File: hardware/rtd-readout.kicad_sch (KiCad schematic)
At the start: 0 parts

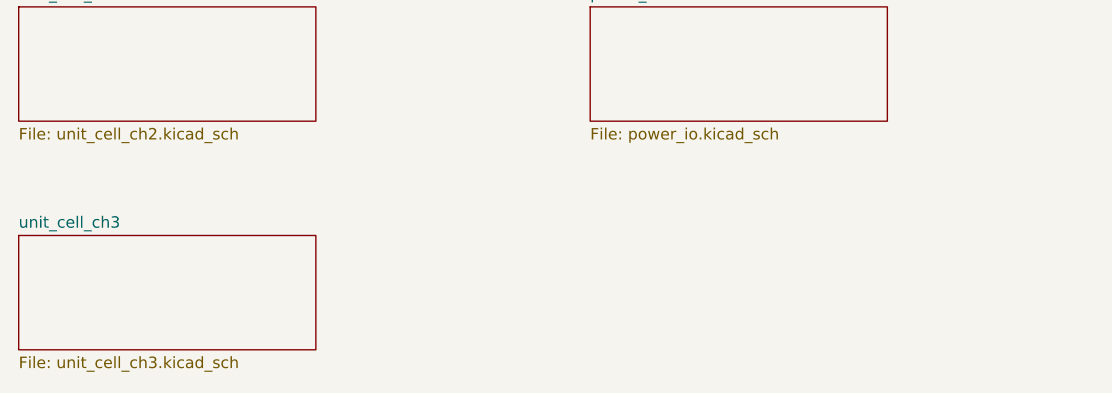
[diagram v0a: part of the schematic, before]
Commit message: trackE: record accepted 3-sheet deviation + clean loose reports artifacts
Integration-review housekeeping (no schematic logic change):
- Mark the three-sheet unit_cell structure as an ACCEPTED deviation in
  docs/sessions/trackE.md, with the consequence noted (a unit-cell change must
  be applied to all three sheets by hand).
- Add a one-line note in root rtd-readout.kicad_sch (title-block comment 2 +
  on-canvas text) so the next reader isn't surprised.
- Remove loose untracked reports/ gate artifacts so the tree is clean for merge.
ERC re-confirmed 0 errors / 0 warnings after the root-sheet edit.

Co-Authored-By: Claude Opus 4.8 <noreply@anthropic.com>
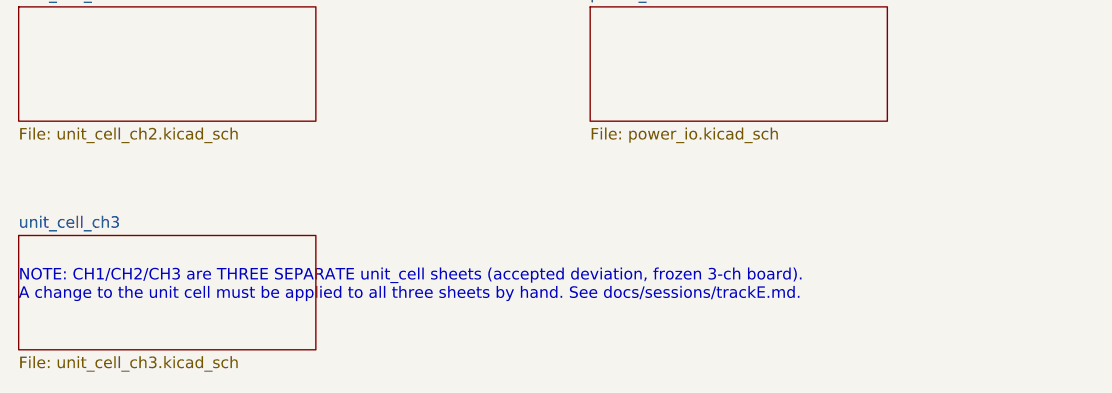
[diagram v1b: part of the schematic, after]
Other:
- note added: "NOTE: CH1/CH2/CH3 are THREE SEPARATE unit_cell sheets (accepted deviation, frozen 3-ch board). A change to the unit cell must be applied to all three sheets by hand. See docs/sessions/trackE.md."
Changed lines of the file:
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@@
 		(rev "A")
 		(comment 1 "Track E schematic; parts from project-local rtd-readout lib (Track A)")
+		(comment 2 "ACCEPTED DEVIATION: three separate unit_cell_chN sheets (not one reused sheet) -- edit each by hand")
+	)
+	(text "NOTE: CH1/CH2/CH3 are THREE SEPARATE unit_cell sheets (accepted deviation, frozen 3-ch board).\nA change to the unit cell must be applied to all three sheets by hand. See docs/sessions/trackE.md."
+		(exclude_from_sim no)
+		(at 25.4 80 0)
+		(effects (font (size 1.27 1.27)) (justify left top))
 	)
 	(sheet

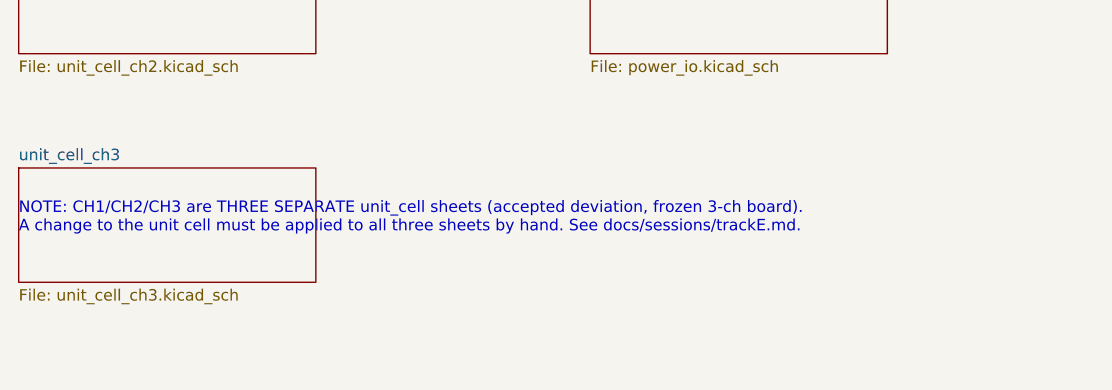
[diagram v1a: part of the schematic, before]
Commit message: trackE: wire-up pass -- drawn wires + power symbols (netlist unchanged)
Convert the label-based capture to a conventionally drawn schematic: unit cells
as a drawn series current-loop (+5V/GND power symbols, CRD->R_ref->RTD, tapped
TOP/MID to TPs+labels); acquisition/power_io pins stub to power symbols/labels;
cross-sheet signals stay labelled. Fixed a y-down rotation bug (CRD anode/cathode
swap) by rotating the CRD 90 not 270.

ERC 0 errors / 0 warnings. Netlist node-for-node IDENTICAL to the pre-wiring
verified netlist (21 nets, diff empty); sim/netlists refreshed.

Co-Authored-By: Claude Opus 4.8 <noreply@anthropic.com>
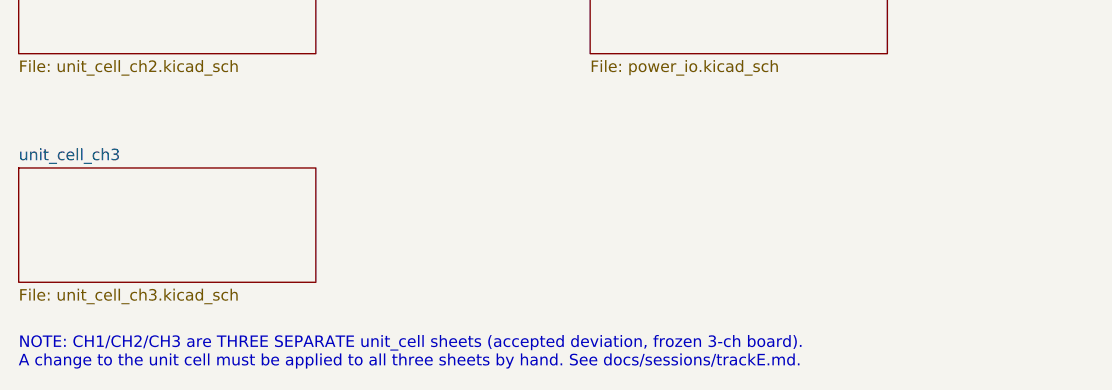
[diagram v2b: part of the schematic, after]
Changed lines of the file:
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@@
 	(text "NOTE: CH1/CH2/CH3 are THREE SEPARATE unit_cell sheets (accepted deviation, frozen 3-ch board).\nA change to the unit cell must be applied to all three sheets by hand. See docs/sessions/trackE.md."
 		(exclude_from_sim no)
-		(at 25.4 80 0)
+		(at 25.4 95 0)
 		(effects (font (size 1.27 1.27)) (justify left top))
 	)

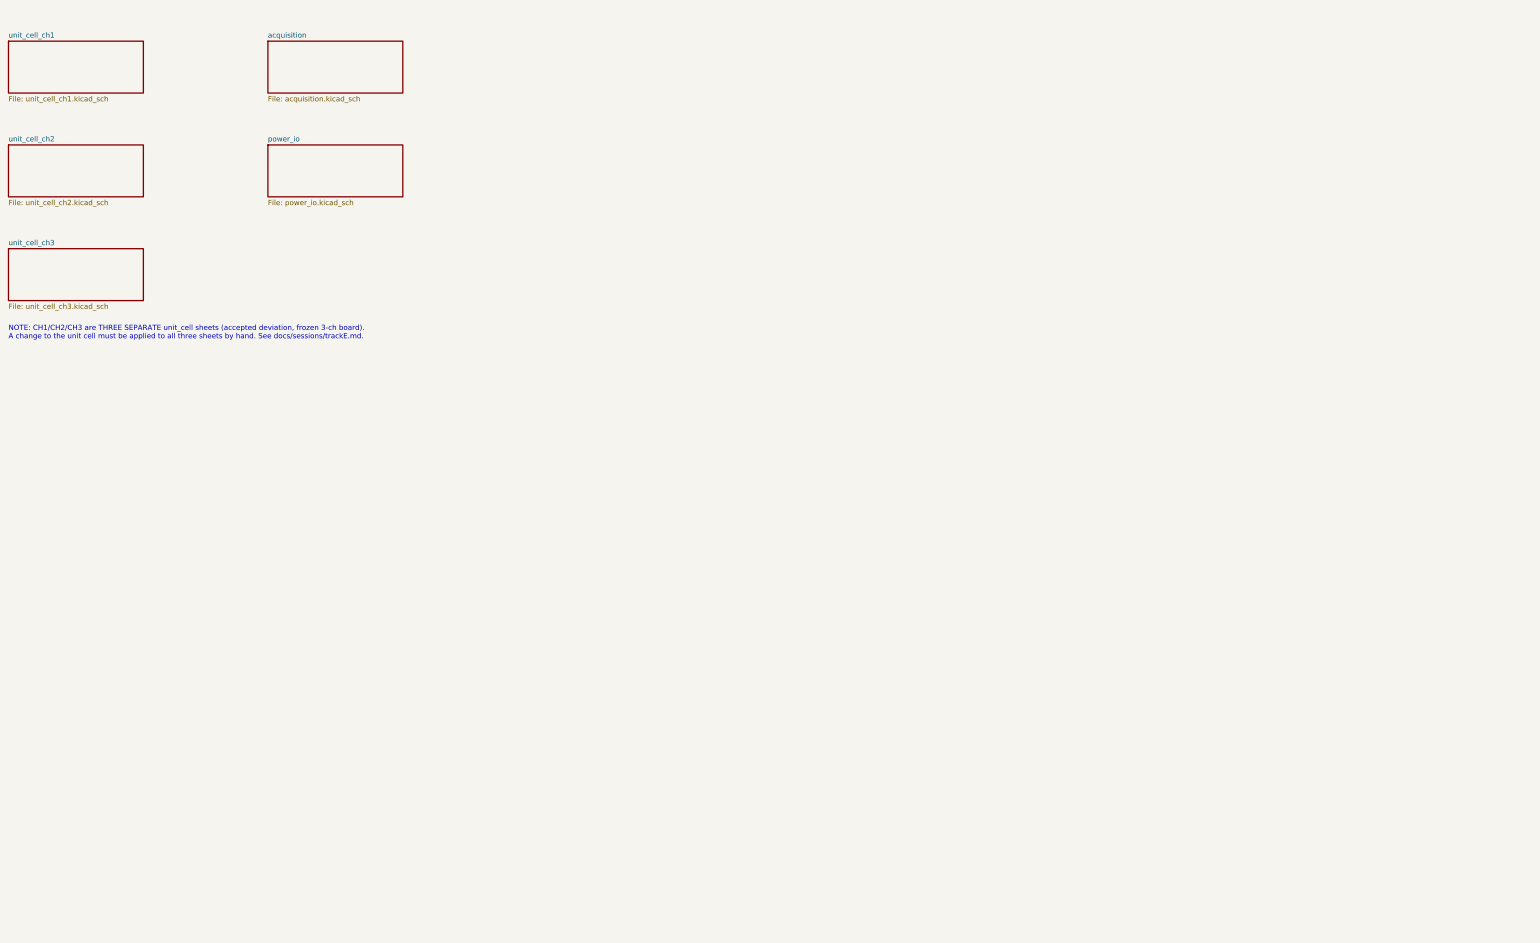
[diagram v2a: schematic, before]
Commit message: schematic: restructure for auditability (page1 = ch1+acquisition+power, drawn wires)
Page 1 merges unit_cell_ch1 + acquisition + power_io with 28 drawn join wires
(CH1 taps -> U1 AIN0/1, Kelvin sense pairs -> J4, I2C bus U1->U2->J5); pages
2-3 = CH2/CH3 cells. Blocks rigidly translated, labels kept: netlist verified
node-for-node IDENTICAL (21 nets, 80 nodes) vs pre-restructure; ERC 0/0; DRC
parity unchanged (47 cosmetic). Verified by 5-agent workflow (independent
netlist oracle, gates, visual audit, BOM byte-identical, adversarial trace);
visual-audit findings fixed (label flips reverted, power-text normalized,
values repositioned, J4 pin names hidden, pages 2-3 title blocks). PCB
untouched (binds by refdes).

Co-Authored-By: Claude Opus 4.8 <noreply@anthropic.com>
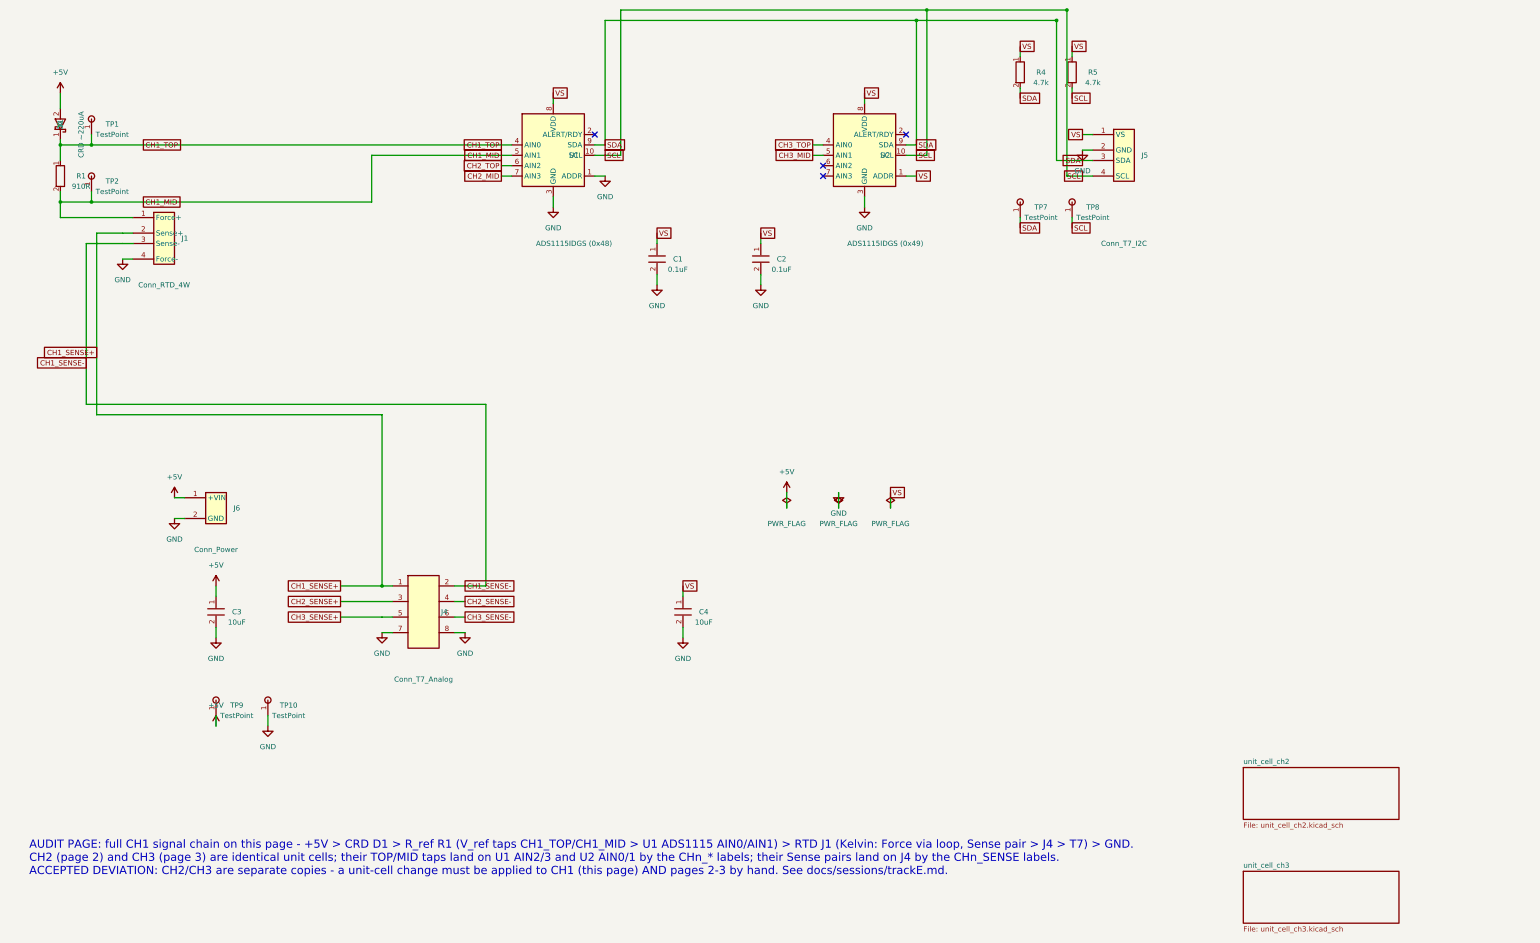
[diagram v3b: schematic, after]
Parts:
- added C1, C2: 0.1uF, rtd-readout:C_0603_1608Metric, symbol rtd-readout:C
- added C3, C4: 10uF, rtd-readout:C_0603_1608Metric, symbol rtd-readout:C
- added D1: CRD ~220uA, rtd-readout:D_MELF, symbol rtd-readout:CRD_1N5283
- added J1: Conn_RTD_4W, rtd-readout:TerminalBlock_Phoenix_MKDS-1,5-4-5.08_1x04_P5.08mm_Horizontal, symbol rtd-readout:Conn_RTD_4W
- added J4: Conn_T7_Analog, rtd-readout:PinHeader_2x04_P2.54mm_Vertical, symbol rtd-readout:Conn_T7_Analog
- added J5: Conn_T7_I2C, rtd-readout:PinHeader_1x04_P2.54mm_Vertical, symbol rtd-readout:Conn_T7_I2C
- added J6: Conn_Power, rtd-readout:TerminalBlock_Phoenix_MKDS-1,5-2-5.08_1x02_P5.08mm_Horizontal, symbol rtd-readout:Conn_Power
- added R1: 910R, rtd-readout:R_1206_3216Metric, symbol rtd-readout:R_ref
- added R4, R5: 4.7k, rtd-readout:R_0805_2012Metric, symbol rtd-readout:R
- added TP1, TP10, TP2, TP7, TP8, TP9: TestPoint, rtd-readout:TestPoint_Pad_D1.5mm, symbol rtd-readout:TestPoint
- added U1: ADS1115IDGS (0x48), rtd-readout:MSOP-10_3x3mm_P0.5mm, symbol rtd-readout:ADS1115
- added U2: ADS1115IDGS (0x49), rtd-readout:MSOP-10_3x3mm_P0.5mm, symbol rtd-readout:ADS1115
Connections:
- new net +5V: C3.1, D1.2 (A), J6.1 (+VIN), TP9.1
- new net CH1_MID: J1.1 (Force+), R1.2, TP2.1, U1.5 (AIN1)
- new net CH1_SENSE+: J1.2 (Sense+), J4.1 (CH1_Sense+)
- new net CH1_SENSE-: J1.3 (Sense-), J4.2 (CH1_Sense-)
- new net CH1_TOP: D1.1 (K), R1.1, TP1.1, U1.4 (AIN0)
- new net CH2_MID: U1.7 (AIN3)
- new net CH2_SENSE+: J4.3 (CH2_Sense+)
- new net CH2_SENSE-: J4.4 (CH2_Sense-)
- new net CH2_TOP: U1.6 (AIN2)
- new net CH3_MID: U2.5 (AIN1)
- new net CH3_SENSE+: J4.5 (CH3_Sense+)
- new net CH3_SENSE-: J4.6 (CH3_Sense-)
- new net CH3_TOP: U2.4 (AIN0)
- new net GND: C1.2, C2.2, C3.2, C4.2, J1.4 (Force-), J4.7 (AGND), J4.8 (AGND), J5.2 (GND), J6.2 (GND), TP10.1, U1.1 (ADDR), U1.3 (GND), U2.3 (GND)
- new net SCL: J5.4 (SCL), R5.2, TP8.1, U1.10 (SCL), U2.10 (SCL)
- new net SDA: J5.3 (SDA), R4.2, TP7.1, U1.9 (SDA), U2.9 (SDA)
- new net VS: C1.1, C2.1, C4.1, J5.1 (VS), R4.1, R5.1, U1.8 (VDD), U2.1 (ADDR), U2.8 (VDD)
- no-connect marks 0 -> 4
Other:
- removed sheet acquisition
- removed sheet power_io
- removed sheet unit_cell_ch1
- note added: "AUDIT PAGE: full CH1 signal chain on this page - +5V > CRD D1 > R_ref R1 (V_ref taps CH1_TOP/CH1_MID > U1 ADS1115 AIN0/AIN1) > RTD J1 (Kelvin: Force via loop, Sense pair > J4 > T7) > GND. CH2 (page 2) and CH3 (page 3) are identical unit cells; their TOP/MID taps land on U1 AIN2/3 and U2 AIN0/1 by the CHn_* labels; their Sense pairs land on J4 by the CHn_SENSE labels. ACCEPTED DEVIATION: CH2/CH3 a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"
- note removed: "NOTE: CH1/CH2/CH3 are THREE SEPARATE unit_cell sheets (accepted deviation, frozen 3-ch board). A change to the unit cell must be applied to all three sheets by hand. See docs/sessions/trackE.md."
- title: RTD Readout Board - 4-wire RTD x3, ratiometric (T7 + ADS1115) -> RTD Readout - 3ch 4-wire RTD, ratiometric

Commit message: rev-C: 4th channel — CH4 on U2's spare AIN2/3, J4 2x5, board grown south
board_spec 3->4ch. Schematic: page 4 (D4/R6/J7/TP11/TP12), U2 AIN2/3 wired,
Conn_T7_Analog 2x5 (CH4 sense on pins 9/10, AGND kept on 7/8); netlist delta
verified exactly the CH4 additions (21->23 nets). Library: 2x05 footprint +
symbol updated (embedded/library kept identical). Layout via pcbnew: board
122x82->122x104, holes moved, planes extended+refilled, CH4 placed/routed,
CH2_SENSE- rerouted off the new J4 row, one VS via relocated. ERC 0/0 (all
severities), DRC 0/0, parity 60 (metadata only), SPICE 7/7. Verified by
5-agent workflow (delta oracle, gates, adversarial layout review incl.
single-point GND tie intact, visual audit 4 pages + board, BOM=35); its
findings (library symbol mismatch, 2 label collisions) fixed and re-gated.

Co-Authored-By: Claude Opus 4.8 <noreply@anthropic.com>
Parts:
- J4: footprint rtd-readout:PinHeader_2x04_P2.54mm_Vertical -> rtd-readout:PinHeader_2x05_P2.54mm_Vertical; MPN PREC004DAAN-RC (2x4; confirm) -> PREC005DAAN-RC (2x5; confirm)
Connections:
- net CH4_TOP: now reaches U2.6 (AIN2)
- net CH4_MID: now reaches U2.7 (AIN3)
- new net CH4_SENSE+: J4.9 (CH4_Sense+)
- new net CH4_SENSE-: J4.10 (CH4_Sense-)
- no-connect marks 4 -> 2
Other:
- added sheet unit_cell_ch4 (unit_cell_ch4.kicad_sch)
- note added: "AUDIT PAGE: full CH1 signal chain on this page - +5V > CRD D1 > R_ref R1 (V_ref taps CH1_TOP/CH1_MID > U1 ADS1115 AIN0/AIN1) > RTD J1 (Kelvin: Force via loop, Sense pair > J4 > T7) > GND. CH2-CH4 (pages 2-4) are identical unit cells; TOP/MID taps land on U1 AIN2/3 (CH2), U2 AIN0/1 (CH3), U2 AIN2/3 (CH4); Sense pairs land on J4 (CH4 on pins 9/10) by the CHn_* labels. ACCEPTED DEVIATION: CH2-CH4 ar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"
- note removed: "AUDIT PAGE: full CH1 signal chain on this page - +5V > CRD D1 > R_ref R1 (V_ref taps CH1_TOP/CH1_MID > U1 ADS1115 AIN0/AIN1) > RTD J1 (Kelvin: Force via loop, Sense pair > J4 > T7) > GND. CH2 (page 2) and CH3 (page 3) are identical unit cells; their TOP/MID taps land on U1 AIN2/3 and U2 AIN0/1 by the CHn_* labels; their Sense pairs land on J4 by the CHn_SENSE labels. ACCEPTED DEVIATION: CH2/CH3 a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"
- title: RTD Readout - 3ch 4-wire RTD, ratiometric -> RTD Readout - 4ch 4-wire RTD, ratiometric
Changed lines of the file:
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@@
 	(paper "A3")
 	(title_block
-		(title "RTD Readout - 3ch 4-wire RTD, ratiometric")
+		(title "RTD Readout - 4ch 4-wire RTD, ratiometric")
 		(rev "B")
 		(comment 1 "Page 1: CH1 unit cell + acquisition + power/IO, drawn wires (audit view)")
-		(comment 2 "Pages 2-3: CH2/CH3 unit cells (separate copies - edit all three by hand)")
-	)
-	(text "AUDIT PAGE: full CH1 signal chain on this page - +5V > CRD D1 > R_ref R1 (V_ref taps CH1_TOP/CH1_MID > U1 ADS1115 AIN0/AIN1) > RTD J1 (Kelvin: Force via loop, Sense pair > J4 > T7) > GND.\nCH2 (page 2) and CH3 (page 3) are identical unit cells; their TOP/MID taps land on U1 AIN2/3 and U2 AIN0/1 by the CHn_* labels; their Sense pairs land on J4 by the CHn_SENSE labels.\nACCEPTED DEVIATION: CH2/CH3 are separate copies - a unit-cell change must be applied to CH1 (this page) AND pages 2-3 by hand. See docs/sessions/trackE.md."
+		(comment 2 "Pages 2-4: CH2-CH4 unit cells (separate copies - edit all four by hand)")
+	)
+	(text "AUDIT PAGE: full CH1 signal chain on this page - +5V > CRD D1 > R_ref R1 (V_ref taps CH1_TOP/CH1_MID > U1 ADS1115 AIN0/AIN1) > RTD J1 (Kelvin: Force via loop, Sense pair > J4 > T7) > GND.\nCH2-CH4 (pages 2-4) are identical unit cells; TOP/MID taps land on U1 AIN2/3 (CH2), U2 AIN0/1 (CH3), U2 AIN2/3 (CH4); Sense pairs land on J4 (CH4 on pins 9/10) by the CHn_* labels.\nACCEPTED DEVIATION: CH2-CH4 are separate copies - a unit-cell change must be applied to CH1 (this page) AND pages 2-4 by hand. See docs/sessions/trackE.md."
 		(exclude_from_sim no)
 		(at 30.48 220.98 0)
@@
 		(effects (font (size 1.27 1.27)) (justify right))
 		(property "Intersheetrefs" "${INTERSHEET_REFS}" (at 222.25 53.34 0) (effects (font (size 1.27 1.27)) (hide yes))))
-(no_connect (at 224.79 55.88))
-(no_connect (at 224.79 58.42))
 (wire (pts (xy 234.95 40.64) (xy 234.95 38.1)) (stroke (width 0) (type default)))
 (global_label "VS" (shape passive) (at 234.95 38.1 0)
@@
 		)
 		(property "Value" "Conn_T7_Analog"
-			(at 127 181.61 0)
-			(show_name no)
-			(do_not_autoplace no)
-			(effects
-				(font
-					(size 1.27 1.27)
-				)
-			)
-		)
-		(property "Footprint" "rtd-readout:PinHeader_2x04_P2.54mm_Vertical"
+			(at 127 184.15 0)
+			(show_name no)
+			(do_not_autoplace no)
+			(effects
+				(font
+					(size 1.27 1.27)
+				)
+			)
+		)
+		(property "Footprint" "rtd-readout:PinHeader_2x05_P2.54mm_Vertical"
 			(at 127 165.1 0)
 			(show_name no)
@@
 			)
 		)
-		(property "MPN" "PREC004DAAN-RC (2x4; confirm)"
+		(property "MPN" "PREC005DAAN-RC (2x5; confirm)"
 			(at 127 165.1 0)
 			(show_name no)
@@
 		(pin "6")
 		(pin "7")
+		(pin "9")
+		(pin "10")
 		(pin "8")
 		(instances (project "rtd-readout" (path "/6ce05a31-b5af-4e3a-a08f-83802c091454" (reference "J4") (unit 1))))
@@
 		(instances (project "rtd-readout" (path "/6ce05a31-b5af-4e3a-a08f-83802c091454" (page "3"))))
 	)
-	(sheet_instances
+	(wire (pts (xy 222.25 55.88) (xy 224.79 55.88)) (stroke (width 0) (type default)))
+(global_label "CH4_TOP" (shape passive) (at 222.25 55.88 0)
+		(effects (font (size 1.27 1.27)) (justify right))
+		(property "Intersheetrefs" "${INTERSHEET_REFS}" (at 222.25 55.88 0) (effects (font (size 1.27 1.27)) (hide yes))))
+(wire (pts (xy 222.25 58.42) (xy 224.79 58.42)) (stroke (width 0) (type default)))
+(global_label "CH4_MID" (shape passive) (at 222.25 58.42 0)
+		(effects (font (size 1.27 1.27)) (justify right))
+		(property "Intersheetrefs" "${INTERSHEET_REFS}" (at 222.25 58.42 0) (effects (font (size 1.27 1.27)) (hide yes))))
+(wire (pts (xy 119.38 173.99) (xy 116.84 173.99)) (stroke (width 0) (type default)))
+(global_label "CH4_SENSE+" (shape passive) (at 106.68 173.99 0)
+		(effects (font (size 1.27 1.27)) (justify right))
+		(property "Intersheetrefs" "${INTERSHEET_REFS}" (at 106.68 173.99 0) (effects (font (size 1.27 1.27)) (hide yes))))
+(wire (pts (xy 134.62 173.99) (xy 137.16 173.99)) (stroke (width 0) (type default)))
+(wire (pts (xy 137.16 173.99) (xy 147.32 173.99)) (stroke (width 0) (type default)))
+(global_label "CH4_SENSE-" (shape passive) (at 147.32 173.99 0)
+		(effects (font (size 1.27 1.27)) (justify left))
+		(property "Intersheetrefs" "${INTERSHEET_REFS}" (at 147.32 173.99 0) (effects (font (size 1.27 1.27)) (hide yes))))
+	(sheet
+		(at 372.11 203.2)
+		(size 38.1 12.7)
+		(exclude_from_sim no)
+		(in_bom yes)
+		(on_board yes)
+		(dnp no)
+		(fields_autoplaced yes)
+		(stroke (width 0.1524) (type solid))
+		(fill (color 0 0 0 0.0000))
+		(property "Sheetname" "unit_cell_ch4" (at 372.11 202.4884 0) (effects (font (size 1.27 1.27)) (justify left bottom)))
+		(property "Sheetfile" "unit_cell_ch4.kicad_sch" (at 372.11 216.6 0) (effects (font (size 1.27 1.27)) (justify left top)))
+		(instances (project "rtd-readout" (path "/6ce05a31-b5af-4e3a-a08f-83802c091454" (page "4"))))
+	)
+(wire (pts (xy 116.84 173.99) (xy 106.68 173.99)) (stroke (width 0) (type default)))
+(sheet_instances
 		(path "/" (page "1"))
 	)
